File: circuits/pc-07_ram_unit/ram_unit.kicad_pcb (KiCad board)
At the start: 2 copper layers, 99.1 x 99.1 mm, 12 parts, among them U5 74HC138, U6 4011

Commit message: pc-08: decoder unit
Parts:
- removed U6: 4011, Package_DIP:DIP-14_W7.62mm_LongPads
- moved U5 18.9 mm to (122.6, 90.8), turned to -90 degrees
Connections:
- DATA_BUS1 pad 10: /mem_write -> /~{mem_write}
- U1 pad 27: /~{write_pulse} -> /~{mem_write}
- U2 pad 27: /~{write_pulse} -> /~{mem_write}
- U3 pad 27: /~{write_pulse} -> /~{mem_write}
- U4 pad 27: /~{write_pulse} -> /~{mem_write}
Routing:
- net /~{mem_write}: track 0.00 -> 89.8 mm
- net /clock: track 63.0 -> 0.00 mm
- net /~{write_pulse}: track 57.7 -> 0.00 mm
- net /mem_write: track 57.4 -> 0.00 mm
- net /adr13: track 65.1 -> 44.4 mm
- net VCC: track 196.0 -> 178.9 mm
- net /adr14: track 55.7 -> 38.9 mm
- net /adr15: track 57.9 -> 46.1 mm
- net /~{ram2}: track 55.1 -> 64.1 mm
- net /~{ram1}: track 47.3 -> 53.8 mm
- net /~{ram0}: track 37.7 -> 43.3 mm
- net /~{ram3}: track 74.5 -> 73.2 mm
- net GND: vias 0 -> 3

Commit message: bus spy, mock orchestrator & cleanup
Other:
- board text added: "74138 (3-8 DECODER)"
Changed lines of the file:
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@@
+		)
+	)
+	(gr_text "74138 (3-8 DECODER)"
+		(at 113.665 94.615 0)
+		(layer "F.SilkS")
+		(effects
+			(font
+				(size 1 1)
+				(thickness 0.1)
+			)
 		)
 	)

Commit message: add filter and decoupling capacitors to all boards
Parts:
- added C1: C_Polarized, Capacitor_SMD:CP_Elec_5x5.3, F.Cu at (64.4, 39.4)
- added C2: C, Capacitor_SMD:C_0603_1608Metric, F.Cu at (90.2, 86.5)
- added C3: C, Capacitor_SMD:C_0603_1608Metric, F.Cu at (77.5, 86.5)
- added C4: C, Capacitor_SMD:C_0603_1608Metric, F.Cu at (64.8, 86.5)
- added C5: C, Capacitor_SMD:C_0603_1608Metric, F.Cu at (102.9, 86.5)
- added C6: C, Capacitor_SMD:C_0603_1608Metric, F.Cu at (121.8, 102.2)
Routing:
- net VCC: track 178.9 -> 208.2 mm
- net GND: vias 3 -> 6

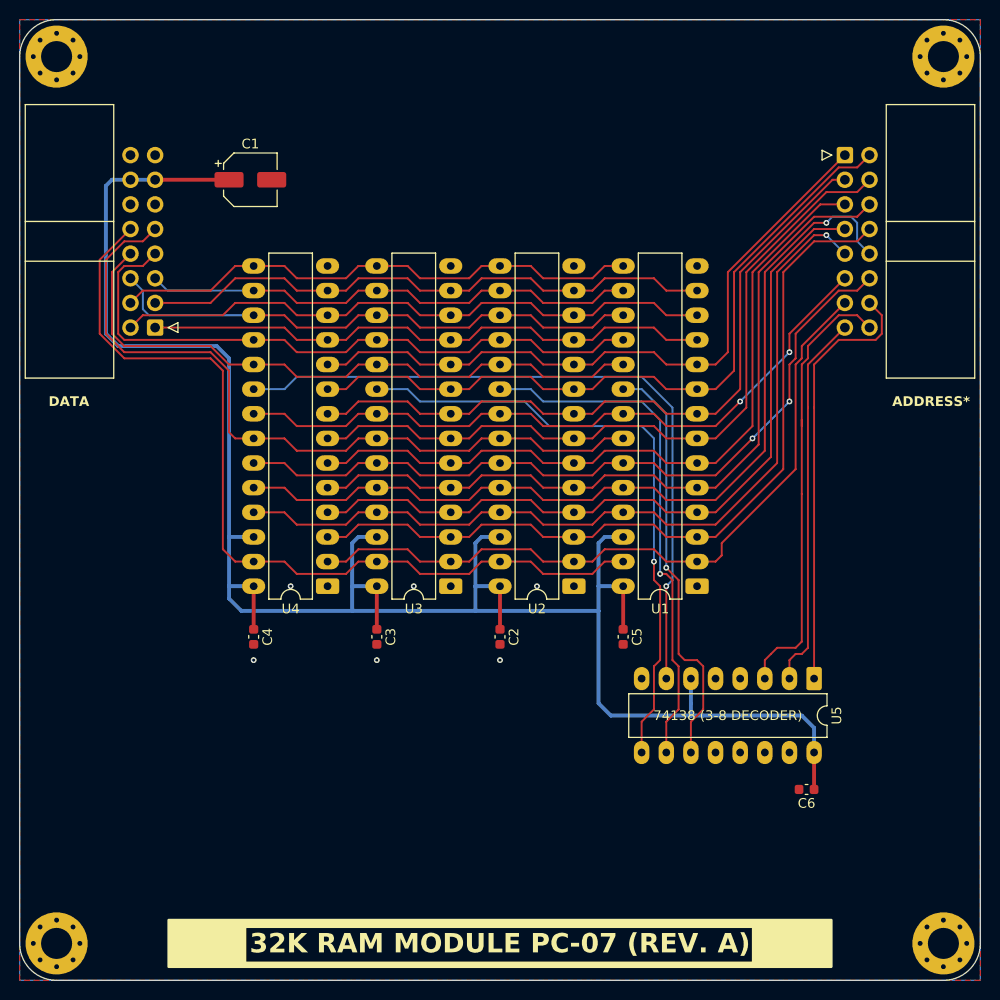
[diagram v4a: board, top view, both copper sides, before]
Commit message: PC-07: reworked RAM unit: falling edge of !mem_write signal is converted to a low-pulse.
In experiments, 2 ceramic caps of 100nF each in series, and 2 resistors of 150 ohms yielded pulse widths of a just a few microseconds at clock rates of up to 25 kHz.
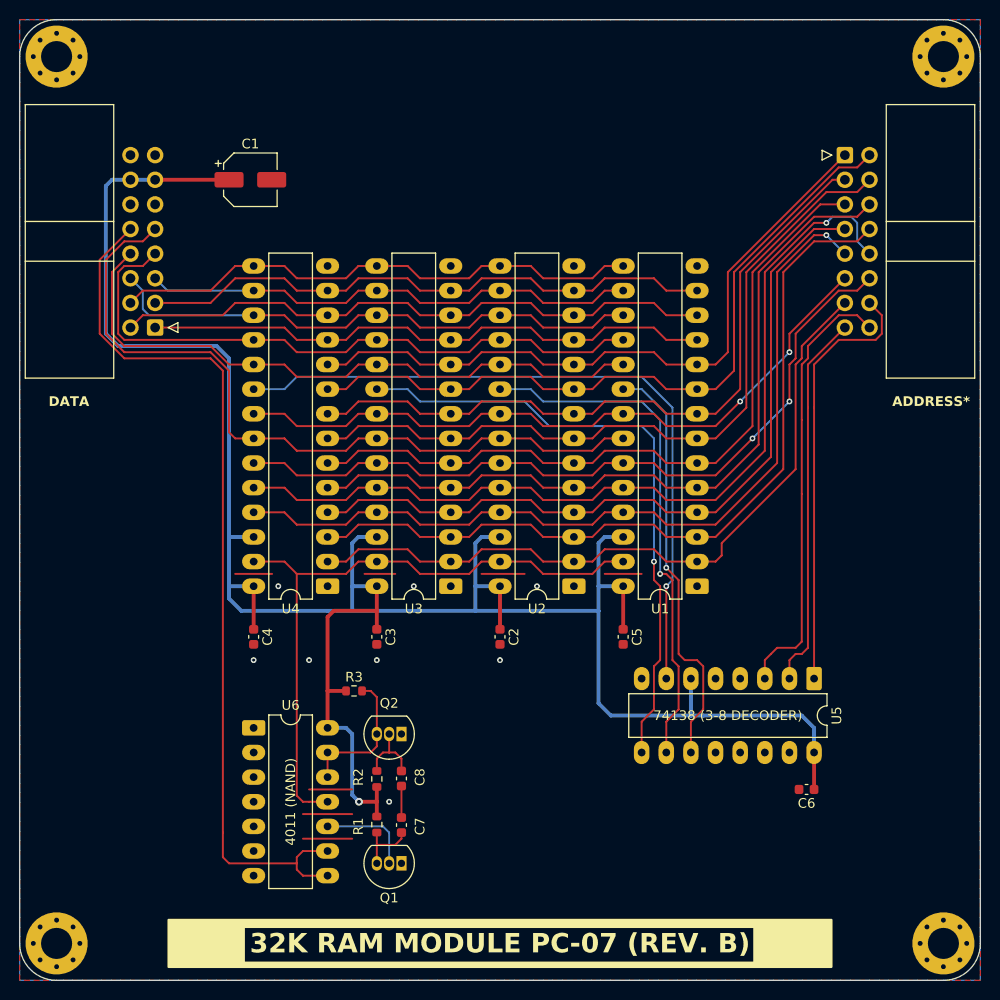
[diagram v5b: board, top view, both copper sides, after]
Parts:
- added C7: 100nF, Capacitor_SMD:C_0603_1608Metric, F.Cu at (80.0, 105.9)
- added C8: 100nF, Capacitor_SMD:C_0603_1608Metric, F.Cu at (80.0, 101.1)
- added Q1: 2N7000, Package_TO_SOT_THT:TO-92_Inline, F.Cu at (80.0, 109.9)
- added Q2: 2N7000, Package_TO_SOT_THT:TO-92_Inline, F.Cu at (80.0, 96.5)
- added R1: 150R, Resistor_SMD:R_0603_1608Metric, F.Cu at (77.5, 105.9)
- added R2: 150R, Resistor_SMD:R_0603_1608Metric, F.Cu at (77.5, 101.2)
- added R3: 1k, Resistor_SMD:R_0603_1608Metric, F.Cu at (75.1, 92.1)
- added U6: 4011, Package_DIP:DIP-14_W7.62mm_LongPads, F.Cu at (64.8, 95.9)
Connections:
- U1 pad 27: /~{mem_write} -> /~{write_pulse}
- U2 pad 27: /~{mem_write} -> /~{write_pulse}
- U3 pad 27: /~{mem_write} -> /~{write_pulse}
- U4 pad 27: /~{mem_write} -> /~{write_pulse}
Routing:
- net /~{write_pulse}: track 0.00 -> 67.6 mm
- net VCC: track 208.2 -> 241.8 mm, vias 0 -> 1
- net GND: track 0.00 -> 29.8 mm, vias 6 -> 8
- net Net-(Q2-D): track 0.00 -> 14.8 mm
- net Net-(Q1-G): track 0.00 -> 9.79 mm
- net Net-(Q2-G): track 0.00 -> 7.51 mm
- net Net-(Q1-D): track 0.00 -> 6.61 mm
- net Net-(C7-Pad2): track 0.00 -> 3.25 mm
- net /~{mem_write}: track 89.8 -> 92.6 mm
- net /adr15: track 46.1 -> 45.4 mm
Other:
- board text added: "32K RAM MODULE PC-07 (REV. B)"
- board text added: "4011 (NAND)"
- board text removed: "32K RAM MODULE PC-07 (REV. A)"

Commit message: pcb design
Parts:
- removed U6: 4011, Package_DIP:DIP-14_W7.62mm_LongPads
- added U7: 74HC14, Package_DIP:DIP-14_W7.62mm, F.Cu at (64.8, 95.9)
- Q1, Q2: footprint Package_TO_SOT_THT:TO-92_Inline -> Package_TO_SOT_THT:TO-92_Inline_Wide
- moved Q1 1.27 mm to (81.3, 109.9)
- moved Q2 1.27 mm to (81.3, 96.5)
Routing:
- net GND: track 29.8 -> 15.2 mm
- net /~{mem_write}: track 92.6 -> 79.8 mm
- net Net-(Q2-D): track 14.8 -> 9.89 mm
- net /~{write_pulse}: track 67.6 -> 65.0 mm
- net Net-(Q1-D): track 6.61 -> 7.14 mm
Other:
- board text added: "7414 (SCHMITT INVERTER)"
- board text removed: "4011 (NAND)"
